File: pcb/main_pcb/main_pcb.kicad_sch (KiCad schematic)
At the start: 0 parts

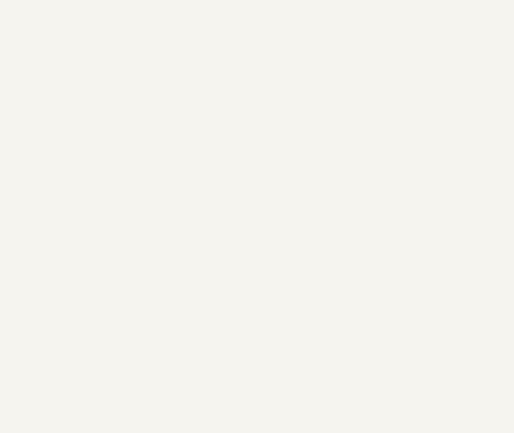
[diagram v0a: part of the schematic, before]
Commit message: Annotate & begin footprint assignment
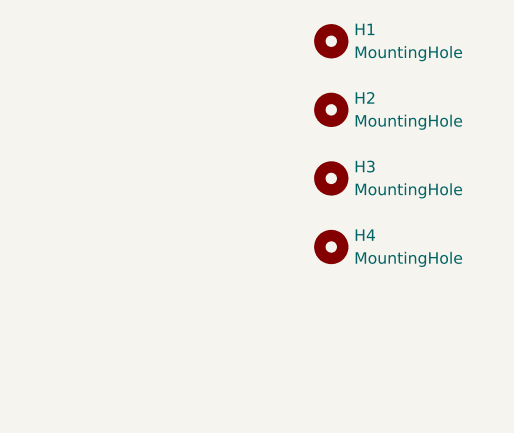
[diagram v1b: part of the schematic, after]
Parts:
- added H1, H2, H3, H4: MountingHole, MountingHole:MountingHole_3.2mm_M3, symbol Mechanical:MountingHole

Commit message: Complete routing and Silkscreen
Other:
- note added: "CWRUbotix"
- note added: "Sponsored By:"
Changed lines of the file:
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@@
 (kicad_sch (version 20211123) (generator eeschema)
   (paper "B")
+  (text "Sponsored By:" (at 298.45 164.465 0)
+    (effects (font (size 5.08 5.08) (thickness 1.016) bold italic) (justify left bottom))
+  )
+  (text "CWRUbotix" (at 363.22 139.065 0)
+    (effects (font (size 5.08 5.08) (thickness 1.016) bold italic) (justify left bottom))
+  )
   (symbol (lib_id "Mechanical:MountingHole") (at 260.35 73.66 0) (unit 1)
     (in_bom yes) (on_board yes) (fields_autoplaced)
@@
     )
   )
+  (symbol (lib_id "LOGO_cwrubotix:LOGO") (at 383.54 109.22 0) (unit 1)
+    (in_bom no) (on_board yes) (fields_autoplaced)
+    (property "Reference" "#G2" (id 0) (at 383.54 89.8429 0)
+      (effects (font (size 1.27 1.27)) hide)
+    )
+    (property "Value" "LOGO" (id 1) (at 383.54 128.5971 0)
+      (effects (font (size 1.27 1.27)) hide)
+    )
+    (property "Footprint" "custom_footprints:LOGO_cwrubotix" (id 2) (at 383.54 109.22 0)
+      (effects (font (size 1.27 1.27)) hide)
+    )
+    (property "Datasheet" "" (id 3) (at 383.54 109.22 0)
+      (effects (font (size 1.27 1.27)) hide)
+    )
+  )
   (symbol (lib_id "Mechanical:MountingHole") (at 260.35 66.04 0) (unit 1)
     (in_bom yes) (on_board yes) (fields_autoplaced)
@@
     )
     (property "Datasheet" "~" (id 3) (at 260.35 58.42 0)
+      (effects (font (size 1.27 1.27)) hide)
+    )
+  )
+  (symbol (lib_id "LOGO_pololu:LOGO") (at 327.025 200.025 0) (unit 1)
+    (in_bom yes) (on_board yes) (fields_autoplaced)
+    (property "Reference" "#G1" (id 0) (at 327.025 170.5683 0)
+      (effects (font (size 1.27 1.27)) hide)
+    )
+    (property "Value" "LOGO" (id 1) (at 327.025 229.4817 0)
+      (effects (font (size 1.27 1.27)) hide)
+    )
+    (property "Footprint" "custom_footprints:LOGO_pololu" (id 2) (at 327.025 200.025 0)
+      (effects (font (size 1.27 1.27)) hide)
+    )
+    (property "Datasheet" "" (id 3) (at 327.025 200.025 0)
       (effects (font (size 1.27 1.27)) hide)
     )
@@
       (reference "#FLG0101") (unit 1) (value "PWR_FLAG") (footprint "")
     )
+    (path "/e5184b65-2d26-49d2-97f9-48c3baaa26ed"
+      (reference "#G1") (unit 1) (value "LOGO") (footprint "custom_footprints:LOGO_pololu")
+    )
+    (path "/97ed0698-ffb5-423c-b4f8-f16c330dcfad"
+      (reference "#G2") (unit 1) (value "LOGO") (footprint "custom_footprints:LOGO_cwrubotix")
+    )
     (path "/4e618dfb-828b-44a9-b1f3-249375cca950/df9d4fc6-e919-46e4-b146-d1882acf53c5"
       (reference "#PWR01") (unit 1) (value "+3V3") (footprint "")
@@
       (reference "#PWR050") (unit 1) (value "+3V3") (footprint "")
     )
+    (path "/4e618dfb-828b-44a9-b1f3-249375cca950/ed161b67-9c6d-49a4-8890-3f9296005132"
+      (reference "#PWR051") (unit 1) (value "GND") (footprint "")
+    )
     (path "/922e5fdd-f699-4ece-8b2c-9b27e43cb136/2cf22679-c886-4e3b-92f4-d103493a194b"
       (reference "#PWR0101") (unit 1) (value "+5V") (footprint "")
@@
       (reference "D4") (unit 1) (value "D_Schottky") (footprint "Diode_SMD:D_TUMD2")
     )
+    (path "/4e618dfb-828b-44a9-b1f3-249375cca950/f2a5b9d5-fa82-42b3-9b89-acb0144dd416"
+      (reference "D5") (unit 1) (value "LED") (footprint "LED_THT:LED_D5.0mm")
+    )
+    (path "/4e618dfb-828b-44a9-b1f3-249375cca950/06f686a4-bcb8-4698-b4bf-62c9ded57b06"
+      (reference "D6") (unit 1) (value "LED") (footprint "LED_THT:LED_D5.0mm")
+    )
+    (path "/4e618dfb-828b-44a9-b1f3-249375cca950/1383d02c-225f-41f0-a056-4cea6a9e47fe"
+      (reference "D7") (unit 1) (value "LED") (footprint "LED_THT:LED_D5.0mm")
+    )
+    (path "/4e618dfb-828b-44a9-b1f3-249375cca950/58d89004-b8b2-44ce-83e5-2c45a6335430"
+      (reference "D8") (unit 1) (value "LED") (footprint "LED_THT:LED_D5.0mm")
+    )
     (path "/9ad6c3da-27fa-49df-a1a3-aa5c2d44a284"
       (reference "H1") (unit 1) (value "MountingHole") (footprint "MountingHole:MountingHole_3.2mm_M3")
@@
       (reference "R17") (unit 1) (value "2.2k") (footprint "Resistor_SMD:R_0603_1608Metric_Pad0.98x0.95mm_HandSolder")
     )
+    (path "/4e618dfb-828b-44a9-b1f3-249375cca950/97bab634-b1fd-43e9-8d08-c387af89a23a"
+      (reference "R18") (unit 1) (value "470") (footprint "Resistor_SMD:R_0603_1608Metric_Pad0.98x0.95mm_HandSolder")
+    )
+    (path "/4e618dfb-828b-44a9-b1f3-249375cca950/b6444cde-94af-4b70-b7de-dcf30ca2cbca"
+      (reference "R19") (unit 1) (value "470") (footprint "Resistor_SMD:R_0603_1608Metric_Pad0.98x0.95mm_HandSolder")
+    )
+    (path "/4e618dfb-828b-44a9-b1f3-249375cca950/0d02106d-06c7-45c8-b406-b55d07d4fab2"
+      (reference "R20") (unit 1) (value "470") (footprint "Resistor_SMD:R_0603_1608Metric_Pad0.98x0.95mm_HandSolder")
+    )
+    (path "/4e618dfb-828b-44a9-b1f3-249375cca950/15ce000f-acbb-4e7c-8c6c-054805918f93"
+      (reference "R21") (unit 1) (value "470") (footprint "Resistor_SMD:R_0603_1608Metric_Pad0.98x0.95mm_HandSolder")
+    )
     (path "/922e5fdd-f699-4ece-8b2c-9b27e43cb136/8515732c-2009-40d7-8440-5d7fd68daa38"

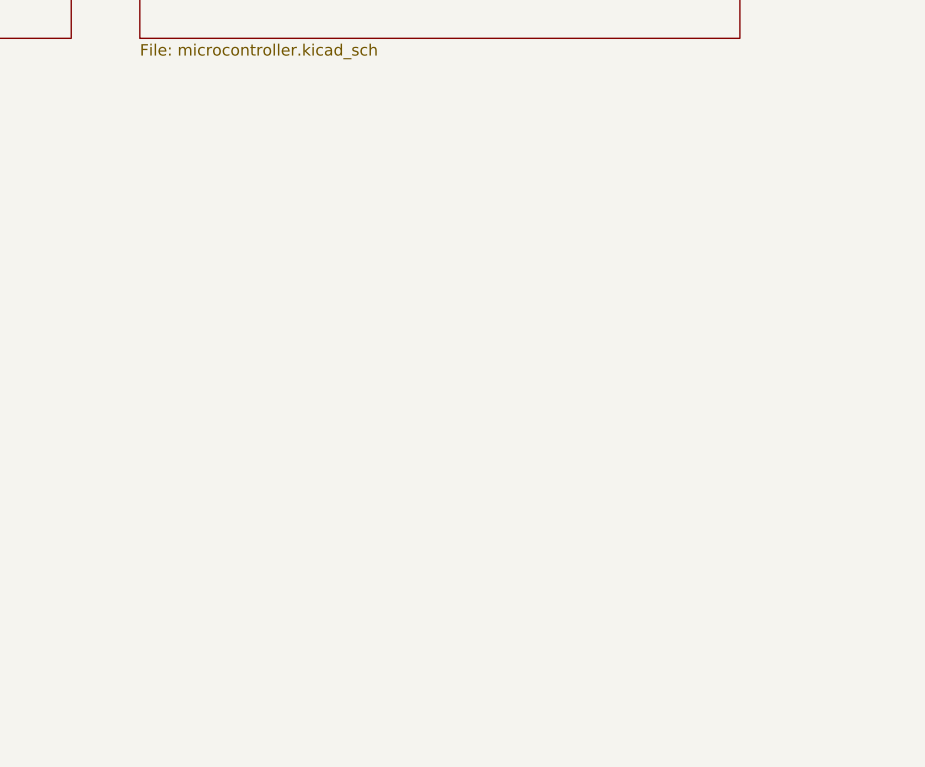
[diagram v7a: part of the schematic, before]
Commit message: Added Teensy 4.0 schematic
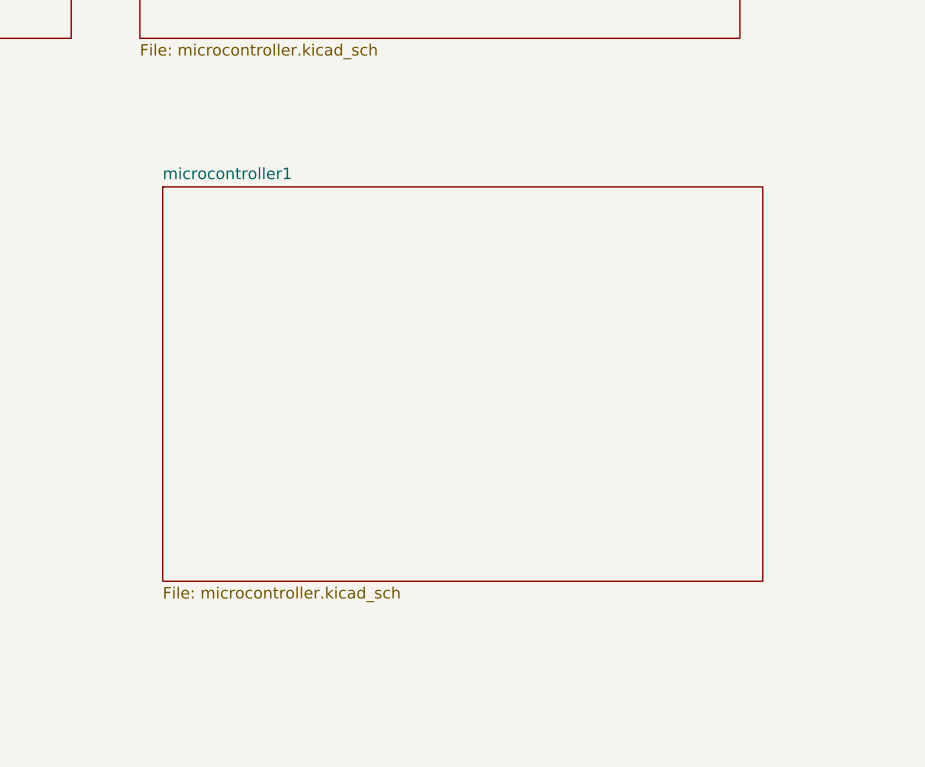
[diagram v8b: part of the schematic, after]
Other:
- added sheet microcontroller1 (microcontroller.kicad_sch)
